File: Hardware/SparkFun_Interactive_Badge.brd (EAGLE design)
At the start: 17.8 x 63.5 mm, 34 parts, among them Q1 DMG2307L, U1 MIC5205-3.3V, U2 ATMEGA328P, U3 CY7C65213, Y1 4MHz

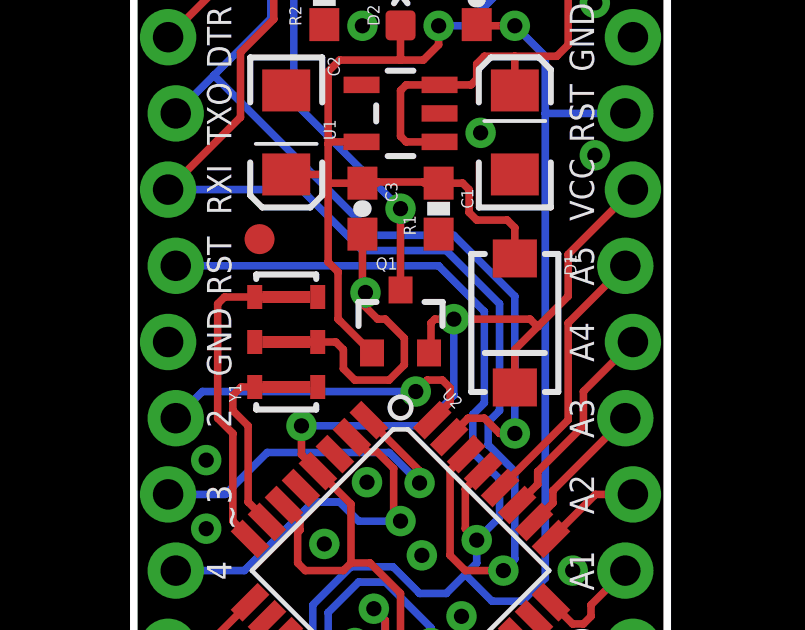
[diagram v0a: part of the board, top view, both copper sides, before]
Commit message: Added badger logo.
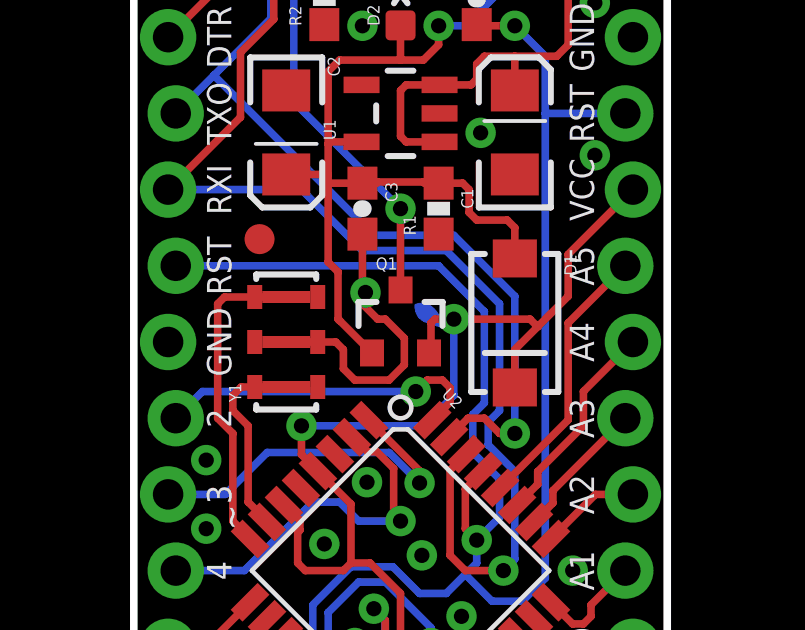
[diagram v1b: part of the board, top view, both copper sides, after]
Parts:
- added U$2: BADGERHACK_LOGODUMMY, SparkFun-Aesthetics:DUMMY
- added U$3: (no value), SparkFun-Aesthetics:HALF_BADGER
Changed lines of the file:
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@@
 <setting verticaltext="up"/>
 </settings>
-<grid distance="0.001" unitdist="inch" unit="inch" style="dots" multiple="1" display="yes" altdistance="0.0001" altunitdist="inch" altunit="inch"/>
+<grid distance="0.05" unitdist="inch" unit="inch" style="dots" multiple="1" display="yes" altdistance="0.005" altunitdist="inch" altunit="inch"/>
 <layers>
-<layer number="1" name="Top" color="4" fill="1" visible="yes" active="yes"/>
+<layer number="1" name="Top" color="4" fill="1" visible="no" active="yes"/>
 <layer number="2" name="Route2" color="1" fill="3" visible="no" active="yes"/>
 <layer number="15" name="Route15" color="4" fill="6" visible="no" active="yes"/>
-<layer number="16" name="Bottom" color="1" fill="1" visible="no" active="yes"/>
+<layer number="16" name="Bottom" color="1" fill="1" visible="yes" active="yes"/>
 <layer number="17" name="Pads" color="2" fill="1" visible="yes" active="yes"/>
 <layer number="18" name="Vias" color="2" fill="1" visible="yes" active="yes"/>
 <layer number="19" name="Unrouted" color="6" fill="1" visible="yes" active="yes"/>
 <layer number="20" name="Dimension" color="15" fill="1" visible="yes" active="yes"/>
-<layer number="21" name="tPlace" color="16" fill="1" visible="yes" active="yes"/>
-<layer number="22" name="bPlace" color="14" fill="1" visible="no" active="yes"/>
-<layer number="23" name="tOrigins" color="15" fill="1" visible="yes" active="yes"/>
-<layer number="24" name="bOrigins" color="15" fill="1" visible="no" active="yes"/>
+<layer number="21" name="tPlace" color="16" fill="1" visible="no" active="yes"/>
+<layer number="22" name="bPlace" color="14" fill="1" visible="yes" active="yes"/>
+<layer number="23" name="tOrigins" color="15" fill="1" visible="no" active="yes"/>
+<layer number="24" name="bOrigins" color="15" fill="1" visible="yes" active="yes"/>
 <layer number="25" name="tNames" color="7" fill="1" visible="no" active="yes"/>
 <layer number="26" name="bNames" color="7" fill="1" visible="no" active="yes"/>
@@
 <attribute name="VALUE" x="6.98" y="24.67" size="0.4064" layer="27" rot="R90"/>
 </element>
+<element name="U$2" library="SparkFun-Aesthetics" package="DUMMY" value="BADGERHACK_LOGODUMMY" x="-60.96" y="-31.75"/>
+<element name="U$3" library="SparkFun-Aesthetics" package="HALF_BADGER" value="" x="12.7" y="20.32" rot="MR0"/>
 </elements>
 <signals>

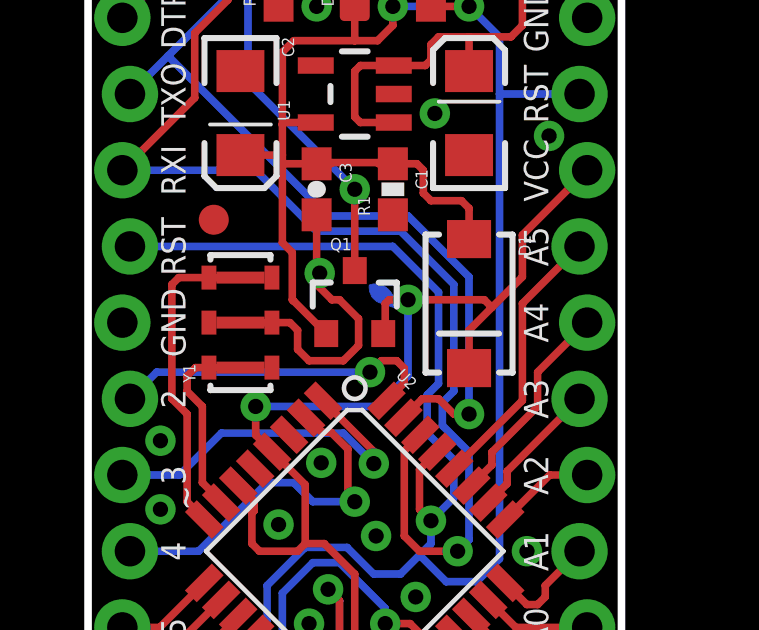
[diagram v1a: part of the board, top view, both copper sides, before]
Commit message: Added half-badger logo.
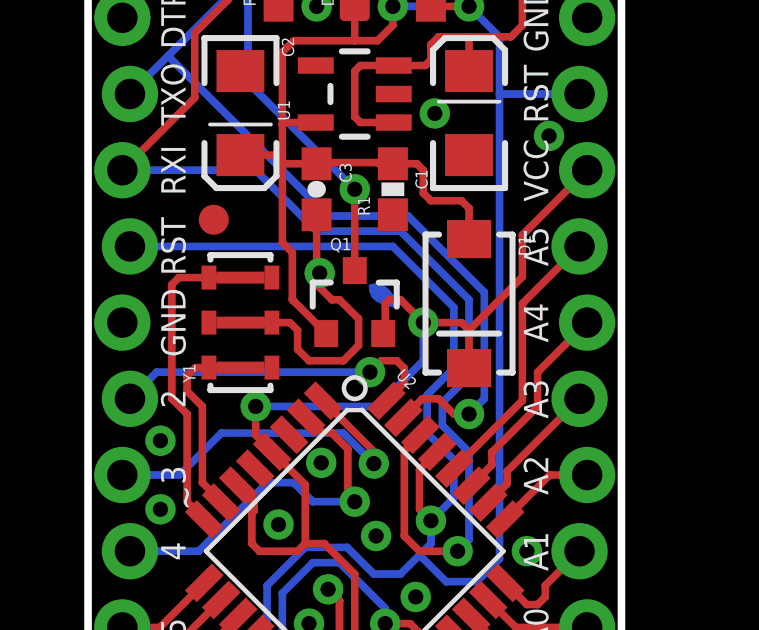
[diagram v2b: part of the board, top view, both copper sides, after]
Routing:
- net VCC: track 49.1 -> 48.1 mm
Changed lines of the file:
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@@
 <grid distance="0.05" unitdist="inch" unit="inch" style="dots" multiple="1" display="yes" altdistance="0.005" altunitdist="inch" altunit="inch"/>
 <layers>
-<layer number="1" name="Top" color="4" fill="1" visible="no" active="yes"/>
+<layer number="1" name="Top" color="4" fill="1" visible="yes" active="yes"/>
 <layer number="2" name="Route2" color="1" fill="3" visible="no" active="yes"/>
 <layer number="15" name="Route15" color="4" fill="6" visible="no" active="yes"/>
@@
 <layer number="19" name="Unrouted" color="6" fill="1" visible="yes" active="yes"/>
 <layer number="20" name="Dimension" color="15" fill="1" visible="yes" active="yes"/>
-<layer number="21" name="tPlace" color="16" fill="1" visible="no" active="yes"/>
+<layer number="21" name="tPlace" color="16" fill="1" visible="yes" active="yes"/>
 <layer number="22" name="bPlace" color="14" fill="1" visible="yes" active="yes"/>
-<layer number="23" name="tOrigins" color="15" fill="1" visible="no" active="yes"/>
+<layer number="23" name="tOrigins" color="15" fill="1" visible="yes" active="yes"/>
 <layer number="24" name="bOrigins" color="15" fill="1" visible="yes" active="yes"/>
 <layer number="25" name="tNames" color="7" fill="1" visible="no" active="yes"/>
@@
 <layer number="43" name="vRestrict" color="2" fill="10" visible="no" active="yes"/>
 <layer number="44" name="Drills" color="7" fill="1" visible="no" active="yes"/>
-<layer number="45" name="Holes" color="7" fill="1" visible="no" active="yes"/>
+<layer number="45" name="Holes" color="7" fill="1" visible="yes" active="yes"/>
 <layer number="46" name="Milling" color="3" fill="1" visible="no" active="yes"/>
-<layer number="51" name="tDocu" color="6" fill="1" visible="no" active="yes"/>
+<layer number="51" name="tDocu" color="6" fill="1" visible="yes" active="yes"/>
 <layer number="52" name="bDocu" color="7" fill="1" visible="no" active="yes"/>
 <layer number="3" name="Route3" color="4" fill="3" visible="no" active="no"/>
@@
 <wire x1="5.588" y1="22.917684375" x2="5.588" y2="23.876" width="0.254" layer="1"/>
 <wire x1="5.588" y1="23.876" x2="9.652" y2="23.876" width="0.254" layer="16"/>
-<wire x1="9.652" y1="23.876" x2="10.668" y2="24.892" width="0.254" layer="16"/>
-<via x="10.668" y="27.432" extent="1-16" drill="0.508"/>
-<wire x1="10.668" y1="27.432" x2="10.033" y2="27.432" width="0.254" layer="1"/>
+<wire x1="9.652" y1="23.876" x2="11.176" y2="25.4" width="0.254" layer="16"/>
+<via x="11.176" y="26.67" extent="1-16" drill="0.508"/>
 <wire x1="10.033" y1="27.432" x2="9.906" y2="27.305" width="0.254" layer="1"/>
 <wire x1="9.906" y1="27.305" x2="9.906" y2="26.371" width="0.254" layer="1"/>
 <wire x1="9.906" y1="26.371" x2="9.84" y2="26.305" width="0.254" layer="1"/>
-<wire x1="10.668" y1="24.892" x2="10.668" y2="27.432" width="0.254" layer="16"/>
 <wire x1="12.7" y1="25.155" x2="12.7" y2="26.416" width="0.254" layer="1"/>
 <wire x1="14.478" y1="28.194" x2="14.478" y2="29.591" width="0.254" layer="1"/>
 <wire x1="14.478" y1="29.591" x2="16.637" y2="31.75" width="0.254" layer="1"/>
-<wire x1="12.7" y1="26.416" x2="13.462" y2="27.178" width="0.254" layer="1"/>
-<wire x1="13.462" y1="27.178" x2="13.208" y2="27.432" width="0.254" layer="1"/>
-<wire x1="13.208" y1="27.432" x2="10.668" y2="27.432" width="0.254" layer="1"/>
-<wire x1="13.462" y1="27.178" x2="14.478" y2="28.194" width="0.254" layer="1"/>
+<wire x1="12.7" y1="26.416" x2="14.478" y2="28.194" width="0.254" layer="1"/>
+<wire x1="10.033" y1="27.432" x2="10.414" y2="27.432" width="0.254" layer="1"/>
+<wire x1="10.414" y1="27.432" x2="11.176" y2="26.67" width="0.254" layer="1"/>
+<wire x1="11.176" y1="25.4" x2="11.176" y2="26.67" width="0.254" layer="16"/>
+<wire x1="11.176" y1="26.67" x2="12.446" y2="26.67" width="0.254" layer="1"/>
+<wire x1="12.446" y1="26.67" x2="12.7" y2="26.416" width="0.254" layer="1"/>
 </signal>
 <signal name="3.3V">
@@
 <wire x1="12.7" y1="37.211" x2="11.469" y2="37.211" width="0.254" layer="1"/>
 <wire x1="11.469" y1="37.211" x2="11.43" y2="37.25" width="0.3048" layer="1"/>
-<wire x1="10.16" y1="29.21" x2="11.684" y2="27.686" width="0.254" layer="16"/>
+<wire x1="10.16" y1="29.21" x2="12.192" y2="27.178" width="0.254" layer="16"/>
 <wire x1="11.43" y1="20.066" x2="11.43" y2="19.304" width="0.254" layer="16"/>
 <wire x1="9.525" y1="18.288" x2="8.636" y2="19.177" width="0.254" layer="16"/>
@@
 <contactref element="JP3" pad="10"/>
 <wire x1="1.397" y1="29.21" x2="10.16" y2="29.21" width="0.254" layer="16"/>
-<wire x1="11.684" y1="27.686" x2="11.684" y2="24.638" width="0.254" layer="16"/>
-<wire x1="11.684" y1="24.638" x2="11.303" y2="24.257" width="0.254" layer="16"/>
 <wire x1="11.303" y1="24.257" x2="11.303" y2="22.987" width="0.254" layer="16"/>
 <wire x1="11.303" y1="22.987" x2="12.192" y2="22.098" width="0.254" layer="16"/>
 <wire x1="12.192" y1="22.098" x2="12.192" y2="20.828" width="0.254" layer="16"/>
 <wire x1="12.192" y1="20.828" x2="11.43" y2="20.066" width="0.254" layer="16"/>
+<wire x1="12.192" y1="27.178" x2="12.192" y2="25.146" width="0.254" layer="16"/>
+<wire x1="12.192" y1="25.146" x2="11.303" y2="24.257" width="0.254" layer="16"/>
 </signal>
 <signal name="DTR">
@@
 <wire x1="3.556" y1="36.322" x2="3.556" y2="34.163" width="0.254" layer="1"/>
 <wire x1="12.7" y1="19.431" x2="12.319" y2="19.05" width="0.254" layer="16"/>
-<wire x1="10.414" y1="29.718" x2="12.192" y2="27.94" width="0.254" layer="16"/>
+<wire x1="10.414" y1="29.718" x2="12.7" y2="27.432" width="0.254" layer="16"/>
 <wire x1="10.414" y1="29.718" x2="7.62" y2="29.718" width="0.254" layer="16"/>
 <wire x1="7.62" y1="29.718" x2="5.588" y2="31.75" width="0.254" layer="16"/>
@@
 <wire x1="1.143" y1="31.75" x2="3.556" y2="34.163" width="0.254" layer="1"/>
 <wire x1="5.588" y1="31.75" x2="1.143" y2="31.75" width="0.254" layer="16"/>
-<wire x1="12.192" y1="27.94" x2="12.192" y2="24.384" width="0.254" layer="16"/>
-<wire x1="12.192" y1="24.384" x2="11.811" y2="24.003" width="0.254" layer="16"/>
 <wire x1="11.811" y1="24.003" x2="11.811" y2="23.241" width="0.254" layer="16"/>
 <wire x1="11.811" y1="23.241" x2="12.7" y2="22.352" width="0.254" layer="16"/>
 <wire x1="12.7" y1="22.352" x2="12.7" y2="19.431" width="0.254" layer="16"/>
+<wire x1="12.7" y1="27.432" x2="12.7" y2="24.892" width="0.254" layer="16"/>
+<wire x1="12.7" y1="24.892" x2="11.811" y2="24.003" width="0.254" layer="16"/>
 </signal>
 <signal name="TXO">
@@
 <wire x1="11.684" y1="24.13" x2="11.141575" y2="24.13" width="0.254" layer="1"/>
 <wire x1="11.141575" y1="24.13" x2="10.5111125" y2="23.4995375" width="0.254" layer="1"/>
-<wire x1="10.668" y1="30.226" x2="12.7" y2="28.194" width="0.254" layer="16"/>
-<wire x1="12.7" y1="28.194" x2="12.7" y2="23.622" width="0.254" layer="16"/>
+<wire x1="10.668" y1="30.226" x2="13.208" y2="27.686" width="0.254" layer="16"/>
 <wire x1="2.667" y1="35.56" x2="4.572" y2="37.465" width="0.254" layer="16"/>
 <wire x1="10.668" y1="30.226" x2="8.001" y2="30.226" width="0.254" layer="16"/>
@@
 <contactref element="JP3" pad="12"/>
 <wire x1="1.397" y1="34.29" x2="2.667" y2="35.56" width="0.254" layer="16"/>
+<wire x1="13.208" y1="27.686" x2="13.208" y2="24.13" width="0.254" layer="16"/>
+<wire x1="13.208" y1="24.13" x2="12.7" y2="23.622" width="0.254" layer="16"/>
 </signal>
 <signal name="D2">

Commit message: Added badge dimensions on custom layer.
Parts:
- moved FRAME1 7.62 mm to (-19.1, -38.1)
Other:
- board text added: "0.13"
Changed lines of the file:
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@@
 <setting verticaltext="up"/>
 </settings>
-<grid distance="0.05" unitdist="inch" unit="inch" style="dots" multiple="1" display="yes" altdistance="0.005" altunitdist="inch" altunit="inch"/>
+<grid distance="0.1" unitdist="inch" unit="inch" style="dots" multiple="1" display="yes" altdistance="0.05" altunitdist="inch" altunit="inch"/>
 <layers>
 <layer number="1" name="Top" color="4" fill="1" visible="yes" active="yes"/>
@@
 <layer number="112" name="tSilk" color="7" fill="1" visible="no" active="no"/>
 <layer number="113" name="IDFDebug" color="4" fill="1" visible="no" active="no"/>
+<layer number="114" name="Badge_Outline" color="11" fill="1" visible="yes" active="yes"/>
 <layer number="116" name="Patch_BOT" color="9" fill="4" visible="no" active="no"/>
 <layer number="121" name="_tsilk" color="7" fill="1" visible="no" active="no"/>
@@
 <wire x1="-11.176" y1="8.89" x2="-12.7" y2="8.89" width="0.254" layer="51"/>
 <wire x1="-11.176" y1="6.35" x2="-12.7" y2="6.35" width="0.254" layer="51"/>
-<dimension x1="-11.43" y1="5.08" x2="0" y2="5.08" x3="-5.715" y3="-3.81" textsize="1.778" textratio="15" layer="51" unit="inch"/>
-<dimension x1="-12.7" y1="6.35" x2="1.27" y2="6.35" x3="-5.715" y3="-7.62" textsize="1.778" textratio="15" layer="51" unit="inch"/>
-<dimension x1="2.794" y1="63.5" x2="14.986" y2="63.5" x3="8.89" y3="67.31" textsize="1.778" textratio="15" layer="51" unit="inch"/>
-<dimension x1="0" y1="48.26" x2="17.78" y2="48.26" x3="8.89" y3="72.39" textsize="1.778" textratio="15" layer="51" unit="inch"/>
-<dimension x1="14.986" y1="63.5" x2="14.986" y2="51.054" x3="22.86" y3="57.277" textsize="1.778" textratio="15" layer="51" unit="inch"/>
-<dimension x1="17.78" y1="48.26" x2="17.78" y2="0" x3="17.78" y3="24.13" textsize="1.778" textratio="15" layer="51" unit="inch"/>
-<dimension x1="17.78" y1="0" x2="17.78" y2="48.26" x3="27.94" y3="24.13" textsize="1.778" textratio="15" layer="51" unit="inch"/>
-<dimension x1="14.986" y1="63.5" x2="15.24" y2="0" x3="33.02" y3="31.75" textsize="1.778" textratio="15" layer="51" dtype="vertical" unit="inch"/>
-<dimension x1="2.54" y1="2.54" x2="15.24" y2="2.54" x3="8.89" y3="-17.78" textsize="1.778" textratio="15" layer="51" dtype="horizontal" unit="inch"/>
-<dimension x1="17.78" y1="0" x2="15.24" y2="2.54" x3="24.13" y3="1.27" textsize="1.778" textratio="15" layer="51" dtype="vertical" unit="inch"/>
-<dimension x1="-13.97" y1="25.4" x2="-11.43" y2="25.4" x3="-12.7" y3="31.75" textsize="1.778" textratio="15" layer="51" dtype="horizontal" unit="inch"/>
-<dimension x1="-17.78" y1="29.21" x2="-54.61" y2="29.21" x3="-36.195" y3="35.56" textsize="1.778" textratio="15" layer="51" dtype="horizontal" unit="inch"/>
-<dimension x1="-11.43" y1="25.4" x2="-54.61" y2="25.4" x3="-33.02" y3="40.64" textsize="1.778" textratio="15" layer="51" dtype="horizontal" unit="inch"/>
-<dimension x1="-54.61" y1="1.27" x2="-54.61" y2="29.21" x3="-58.42" y3="15.24" textsize="1.778" textratio="15" layer="51" dtype="horizontal" unit="inch"/>
 <wire x1="6.35" y1="1.27" x2="6.35" y2="-0.254" width="0.254" layer="51"/>
 <wire x1="8.89" y1="1.27" x2="8.89" y2="-0.254" width="0.254" layer="51"/>
@@
 <wire x1="12.7" y1="-8.636" x2="5.08" y2="-8.636" width="0.254" layer="51"/>
 <wire x1="5.08" y1="-8.636" x2="5.08" y2="-0.254" width="0.254" layer="51"/>
-<dimension x1="12.7" y1="-8.636" x2="5.08" y2="-8.636" x3="8.89" y3="-12.7" textsize="1.778" textratio="15" layer="51" unit="inch"/>
-<dimension x1="12.7" y1="-0.254" x2="12.7" y2="-8.636" x3="20.32" y3="-4.445" textsize="1.778" textratio="15" layer="51" unit="inch"/>
+<wire x1="-48.895" y1="1.905" x2="-48.895" y2="28.575" width="0.254" layer="114"/>
+<wire x1="-48.895" y1="28.575" x2="-18.415" y2="28.575" width="0.254" layer="114"/>
+<wire x1="-18.415" y1="28.575" x2="-18.415" y2="1.905" width="0.254" layer="114"/>
+<wire x1="-18.415" y1="1.905" x2="-48.895" y2="1.905" width="0.254" layer="114"/>
+<wire x1="-85.09" y1="119.38" x2="17.78" y2="119.38" width="0.254" layer="114"/>
+<wire x1="17.78" y1="119.38" x2="17.78" y2="-7.62" width="0.254" layer="114"/>
+<wire x1="17.78" y1="-7.62" x2="-85.09" y2="-7.62" width="0.254" layer="114"/>
+<wire x1="-85.09" y1="-7.62" x2="-85.09" y2="119.38" width="0.254" layer="114"/>
+<wire x1="-67.945" y1="101.6" x2="-67.945" y2="68.58" width="0.254" layer="51"/>
+<wire x1="-67.945" y1="68.58" x2="0.635" y2="68.58" width="0.254" layer="51"/>
+<wire x1="0.635" y1="68.58" x2="0.635" y2="101.6" width="0.254" layer="51"/>
+<wire x1="0.635" y1="101.6" x2="-67.945" y2="101.6" width="0.254" layer="51"/>
+<dimension x1="0" y1="0" x2="6.35" y2="1.27" x3="3.175" y3="-13.97" textsize="1.778" textratio="15" layer="51" dtype="horizontal" unit="inch"/>
+<dimension x1="0" y1="0" x2="17.78" y2="0" x3="8.89" y3="-24.13" textsize="1.778" textratio="15" layer="51" dtype="horizontal" unit="inch"/>
+<dimension x1="0" y1="0" x2="2.54" y2="2.54" x3="1.27" y3="-19.05" textsize="1.778" textratio="15" layer="51" dtype="horizontal" unit="inch"/>
+<dimension x1="0" y1="0" x2="17.78" y2="48.26" x3="31.75" y3="24.13" textsize="1.778" textratio="15" layer="51" dtype="vertical" unit="inch"/>
+<dimension x1="0" y1="0" x2="14.986" y2="51.054" x3="35.56" y3="25.527" textsize="1.778" textratio="15" layer="51" dtype="vertical" unit="inch"/>
+<dimension x1="0" y1="0" x2="14.986" y2="63.5" x3="39.37" y3="31.75" textsize="1.778" textratio="15" layer="51" dtype="vertical" unit="inch"/>
+<dimension x1="17.78" y1="0" x2="15.24" y2="2.54" x3="27.94" y3="1.27" textsize="1.778" textratio="15" layer="51" dtype="vertical" unit="inch"/>
+<dimension x1="0" y1="0" x2="12.7" y2="-8.636" x3="24.13" y3="-4.318" textsize="1.778" textratio="15" layer="51" dtype="vertical" unit="inch"/>
+<dimension x1="0" y1="0" x2="-11.43" y2="5.08" x3="-5.715" y3="1.27" textsize="1.778" textratio="15" layer="51" dtype="horizontal" unit="inch"/>
+<dimension x1="0" y1="0" x2="-17.78" y2="0" x3="-8.89" y3="-3.81" textsize="1.778" textratio="15" layer="51" dtype="horizontal" unit="inch"/>
+<dimension x1="0" y1="0" x2="-54.61" y2="1.27" x3="-27.305" y3="-7.62" textsize="1.778" textratio="15" layer="51" dtype="horizontal" unit="inch"/>
+<dimension x1="0" y1="0" x2="0" y2="5.08" x3="-5.08" y3="2.54" textsize="1.778" textratio="15" layer="51" dtype="vertical" unit="inch"/>
+<dimension x1="0" y1="0" x2="-8.89" y2="25.4" x3="-15.24" y3="12.7" textsize="1.778" textratio="15" layer="51" dtype="vertical" unit="inch"/>
+<dimension x1="16.383" y1="3.683" x2="18.669" y2="5.969" x3="19.05" y3="5.969" textsize="1.778" textratio="15" layer="51" dtype="leader" unit="inch"/>
+<text x="19.304" y="5.969" size="1.778" layer="51" ratio="15" align="center-left">0.13</text>
+<dimension x1="-85.09" y1="-7.62" x2="17.78" y2="-7.62" x3="-33.655" y3="-27.94" textsize="1.778" textratio="15" layer="114" dtype="horizontal" unit="inch"/>
+<dimension x1="-85.09" y1="-7.62" x2="-48.895" y2="1.905" x3="-66.9925" y3="-17.78" textsize="1.778" textratio="15" layer="114" dtype="horizontal" unit="inch"/>
+<dimension x1="-85.09" y1="-7.62" x2="-85.09" y2="119.38" x3="-99.06" y3="55.88" textsize="1.778" textratio="15" layer="114" dtype="horizontal" unit="inch"/>
+<dimension x1="-85.09" y1="-7.62" x2="-18.415" y2="1.905" x3="-51.7525" y3="-22.86" textsize="1.778" textratio="15" layer="114" dtype="horizontal" unit="inch"/>
+<dimension x1="-85.09" y1="-7.62" x2="-48.895" y2="1.905" x3="-88.9" y3="-2.8575" textsize="1.778" textratio="15" layer="114" dtype="vertical" unit="inch"/>
+<dimension x1="-85.09" y1="-7.62" x2="-48.895" y2="28.575" x3="-93.98" y3="10.4775" textsize="1.778" textratio="15" layer="114" dtype="vertical" unit="inch"/>
 </plain>
 <attributes>
@@
 <element name="FID1" library="SparkFun-Aesthetics" package="FIDUCIAL-1X2" value="FIDUCIAL1X2" x="4.191" y="30.099"/>
 <element name="FID2" library="SparkFun-Aesthetics" package="FIDUCIAL-1X2" value="FIDUCIAL1X2" x="15.24" y="49.53"/>
-<element name="FRAME1" library="SparkFun-Aesthetics" package="CREATIVE_COMMONS" value="" x="-19.05" y="-30.48" smashed="yes">
+<element name="FRAME1" library="SparkFun-Aesthetics" package="CREATIVE_COMMONS" value="" x="-19.05" y="-38.1" smashed="yes">
 <attribute name="VERSION" value="v01" x="1.27" y="46.609" size="1.27" layer="16" font="vector" ratio="15" rot="SMR90" align="center"/>
-<attribute name="DESIGNER" value="Shawn Hymel" x="7.62" y="-30.48" size="1.778" layer="51"/>
+<attribute name="DESIGNER" value="Shawn Hymel" x="7.62" y="-38.1" size="1.778" layer="51"/>
 </element>
 <element name="JP1" library="SparkFun-Connectors" package="USB-A-PCB" value="USBPCB" x="8.89" y="58.42" rot="R270"/>
